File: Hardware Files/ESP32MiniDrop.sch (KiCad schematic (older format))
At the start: 47 parts, among them J1 USB_B_Mini, J2 Barrel_Jack, J3 AudioJack3, J4 Solenoid? Terminal, J5 PROGRAMMING, Q1 S8050, Q2 S8050, Q3 NMOS 60V 46A, SW1 SPST (RED), SW2 SPST (BLUE)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

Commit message: Cleanup Schematics
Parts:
- J4: value Solenoid? Terminal -> Solenoid1 Terminal
- J5: value PROGRAMMING -> 0.100\" 2x4 Header
- R1, R10, R13, R16, R2, R6, R7: value 10k -> 10k 1% 0.1W
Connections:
- net labels added: PairSwitch_CTLI
- net labels removed: PairWitch_CTLI
- wire segments 182 -> 179
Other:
- note added: "18A Max"
- note added: "1A Max"
- note added: "A resistor divider (or functionally-equivalent circuit) on VBUS\nis required to reduce input voltage below maximimum. \nIn this case, the current limitation of the resistor divider \nprevents high VBUS pin leakage current, even \nthough the VIO + 2.5 V specification is not strictly met while\nthe device is not powered."
- note added: "Camera Connection"
- note added: "Camera I/O"
- note added: "D7 must be mounted in reverse. Fixed in Rev A02."
- note added: "EN"
- note added: "ERRATA"
- note added: "IO 0"
- note added: "Lowest current rating is for flyback diode, which could see spikes of\ncurrent equal to the operating current of the coil. 5A at 12V provides \nmaximum of 60 Watts. Typical 12v solenoid is 6.5 Watts. \n\nPlan for testing inductive load at 50 Watts for 20% safety margin.\n\nThrough Hole diodes rated at 100V 20A are available, at marginal\nincrase in cost."
- note added: "MCU"
- note added: "Most DSLR cameras have a 2.5mm TRS port on the camera body to\nallow remote Shutter and Focus control. Different models might have\nShutter and Focus switched, so software might require switching pin\nfunction."
- note added: "NOTE:\nNeed to test LED current with no\ncurrent limiting resisitor in place.\nExpect to damage some LEDs"
- note added: "NOTES"
- note added: "Power Input"
- note added: "Programming Header"
- note added: "REV A01"
- note added: "Regulator for both 12V and 5V\ninput sources"
- note added: "Solenoid Control"
- note added: "Status LEDs"
- note added: "Testing USB to UART chip as found on ESP32 Dev Kit to allow for\nautomatic programing with the Arduino IDE. If that fails, back up\nprogramming header can be used, with jumpers to implement\nboot selection"
- note added: "Theoretical Maximum Power for Solenoid"
- note added: "To enter programming mode"
- note added: "U1 Bypass Capacitors"
- note added: "U3 Bypass Capacitors"
- note added: "User Pair Switch"
- note removed: "Regulator for both 12V and 5V"
- moved on the sheet: C1, C2, C3, C4, C5, C6, C7, C8, C9, D1, D2, D3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

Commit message: Update wrong PN for Green LED
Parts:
- D3: MF Wurth -> Wurth Elektronik; MPN MBR120VLSFT3G -> 150120GS75000
- D4: MF Würth Elektronik -> Wurth Elektronik
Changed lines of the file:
@@
 F 2 "LED_SMD:LED_1206_3216Metric_Pad1.42x1.75mm_HandSolder" H 11100 4050 50  0001 C CNN
 F 3 "~" H 11100 4050 50  0001 C CNN
-F 4 "Würth Elektronik" H 11100 4050 50  0001 C CNN "MF"
+F 4 "Wurth Elektronik" H 11100 4050 50  0001 C CNN "MF"
 F 5 "150120BS75000" H 11100 4050 50  0001 C CNN "MPN"
 	1    11100 4050
@@
 F 2 "LED_SMD:LED_1206_3216Metric_Pad1.42x1.75mm_HandSolder" H 11100 3550 50  0001 C CNN
 F 3 "~" H 11100 3550 50  0001 C CNN
-F 4 "Wurth" H 11100 3550 50  0001 C CNN "MF"
-F 5 "MBR120VLSFT3G" H 11100 3550 50  0001 C CNN "MPN"
+F 4 "Wurth Elektronik" H 11100 3550 50  0001 C CNN "MF"
+F 5 "150120GS75000" H 11100 3550 50  0001 C CNN "MPN"
 	1    11100 3550
 	1    0    0    -1

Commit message: Update project footprint library
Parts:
- J2: footprint ESP32 Drop Controller:PJ-037A -> ESP32MiniDrop_PCB_Library:PJ-037A
- J3: footprint ESP32 Drop Controller:STX-3000 -> ESP32MiniDrop_PCB_Library:STX-3000
- J4: footprint ESP32 Drop Controller:1935161 -> ESP32MiniDrop_PCB_Library:1935161
- SW1, SW2: footprint ESP32 Drop Controller:1825027-8 -> ESP32MiniDrop_PCB_Library:1825027-8
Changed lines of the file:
@@
 F 0 "J4" H 13980 6692 50  0000 L CNN
 F 1 "Solenoid1 Terminal" H 13980 6601 50  0000 L CNN
-F 2 "ESP32 Drop Controller:1935161" H 13900 6700 50  0001 C CNN
+F 2 "ESP32MiniDrop_PCB_Library:1935161" H 13900 6700 50  0001 C CNN
 F 3 "~" H 13900 6700 50  0001 C CNN
 F 4 "Pheonix Contact" H 13900 6700 50  0001 C CNN "MF"
@@
 F 0 "SW1" H 4500 6810 50  0000 C CNN
 F 1 "SPST (RED)" H 4500 6719 50  0000 C CNN
-F 2 "ESP32 Drop Controller:1825027-8" H 4500 6725 50  0001 C CNN
+F 2 "ESP32MiniDrop_PCB_Library:1825027-8" H 4500 6725 50  0001 C CNN
 F 3 "~" H 4500 6725 50  0001 C CNN
 F 4 "TE Connectivity ALCOSWITCH Switches" H 4500 6525 50  0001 C CNN "MF"
@@
 F 0 "J2" H 1320 9700 50  0000 R CNN
 F 1 "Barrel_Jack" H 1320 9609 50  0000 R CNN
-F 2 "ESP32 Drop Controller:PJ-037A" H 1600 9610 50  0001 C CNN
+F 2 "ESP32MiniDrop_PCB_Library:PJ-037A" H 1600 9610 50  0001 C CNN
 F 3 "" H 1600 9610 50  0001 C CNN
 F 4 "CUI Devices" H 1550 9650 50  0001 C CNN "MF"
@@
 F 0 "SW2" H 11700 2535 50  0000 C CNN
 F 1 "SPST (BLUE)" H 11700 2444 50  0000 C CNN
-F 2 "ESP32 Drop Controller:1825027-8" H 11700 2450 50  0001 C CNN
+F 2 "ESP32MiniDrop_PCB_Library:1825027-8" H 11700 2450 50  0001 C CNN
 F 3 "~" H 11700 2450 50  0001 C CNN
 F 4 "TE Connectivity ALCOSWITCH Switches" H 11700 2250 50  0001 C CNN "MF"
@@
 F 0 "J3" H 9170 7075 50  0000 R CNN
 F 1 "AudioJack3" H 9170 6984 50  0000 R CNN
-F 2 "ESP32 Drop Controller:STX-3000" H 9450 7050 50  0001 C CNN
+F 2 "ESP32MiniDrop_PCB_Library:STX-3000" H 9450 7050 50  0001 C CNN
 F 3 "~" H 9450 7050 50  0001 C CNN
 F 4 "Kycon, Inc." H 9450 7050 50  0001 C CNN "MF"

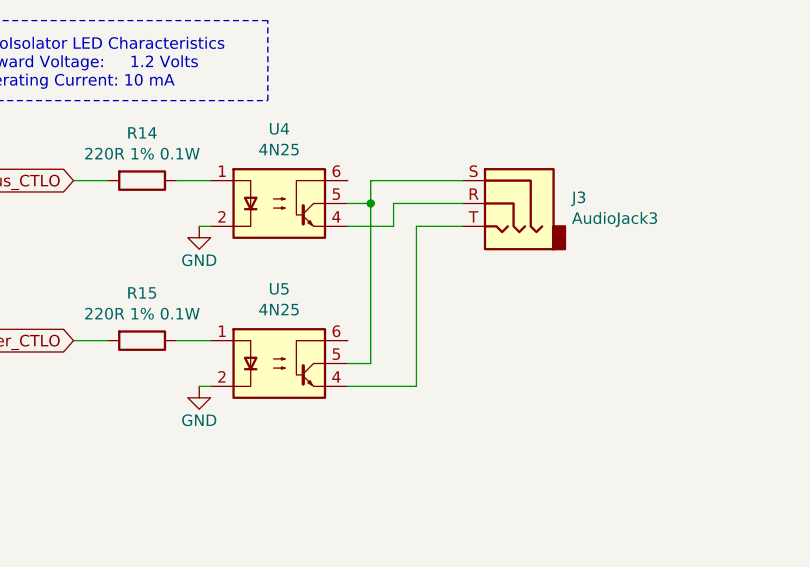
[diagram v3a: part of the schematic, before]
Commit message: fix shutter control hookup
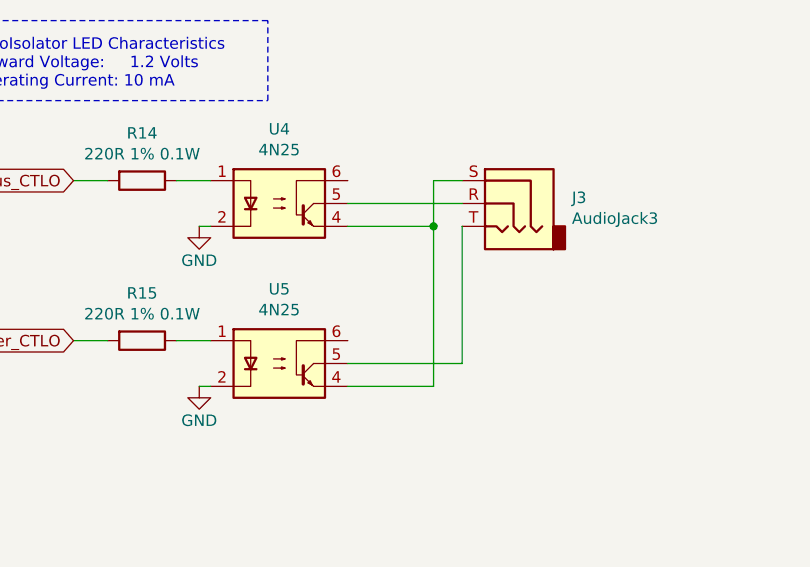
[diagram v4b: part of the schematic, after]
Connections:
- wire segments 179 -> 176
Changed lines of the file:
@@
 	1    0    0    -1
 $EndComp
-Wire Wire Line
-	9250 7050 8950 7050
-Wire Wire Line
-	8950 7050 8950 7150
-Wire Wire Line
-	8950 7150 8750 7150
-Wire Wire Line
-	9250 7150 9050 7150
-Wire Wire Line
-	9050 7850 8750 7850
-Wire Wire Line
-	8750 7750 8850 7750
-Wire Wire Line
-	8850 7050 8750 7050
-Wire Wire Line
-	8850 7050 8850 6950
-Wire Wire Line
-	8850 6950 9250 6950
 Text GLabel 7550 7650 0    50   Input ~ 0
 Shutter_CTLO
@@
 Wire Wire Line
 	8100 7850 8150 7850
-Wire Wire Line
-	8850 7050 8850 7750
-Connection ~ 8850 7050
-Wire Wire Line
-	9050 7150 9050 7850
 Text Notes 7100 6550 0    50   ~ 0
 OptoIsolator LED Characteristics\nForward Voltage:     1.2 Volts\nOperating Current: 10 mA
@@
 Text Notes 11300 4450 0    50   ~ 0
 NOTE:\nNeed to test LED current with no\ncurrent limiting resisitor in place.\nExpect to damage some LEDs
+Wire Wire Line
+	9125 7850 9125 7150
+Wire Wire Line
+	8750 7850 9125 7850
+Wire Wire Line
+	9250 6950 9125 6950
+Wire Wire Line
+	9125 6950 9125 7150
+Connection ~ 9125 7150
+Wire Wire Line
+	8750 7150 9125 7150
+Wire Wire Line
+	8750 7050 9250 7050
+Wire Wire Line
+	9250 7150 9250 7750
+Wire Wire Line
+	9250 7750 8750 7750
 $EndSCHEMATC

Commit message: Fix pin mapping error on Q1, Q2
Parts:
- Q1, Q2: symbol Transistor_BJT:S8050 -> Device:Q_NPN_BEC
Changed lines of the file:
@@
 	950  3500 1000 3500
 $Comp
-L Transistor_BJT:S8050 Q?
+L Device:Q_NPN_BEC Q?
 U 1 1 5F512BB3
 P 1725 6025
@@
 	1825 5825 1825 5775
 $Comp
-L Transistor_BJT:S8050 Q?
+L Device:Q_NPN_BEC Q?
 U 1 1 5F512BC6
 P 1725 6775

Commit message: Change mounting holes to M3, update tracks, change solenoid control to pin 8 of ESP32
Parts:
- added M1, M2, M3, M4: Conn_01x01, MountingHole:MountingHole_3.2mm_M3_ISO7380_Pad, symbol Connector_Generic:Conn_01x01
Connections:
- wire segments 176 -> 184
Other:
- note added: "Mounting Holes"
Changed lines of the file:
@@
 Text GLabel 12850 7350 0    50   Input ~ 0
 Solenoid_1_CTLO
-Text GLabel 9400 3900 2    50   Input ~ 0
+Text GLabel 9400 3700 2    50   Input ~ 0
 Solenoid_1_CTLO
 $Comp
@@
 Wire Wire Line
 	9500 2600 9150 2600
-Wire Wire Line
-	9150 3900 9400 3900
 Text Label 4875 2850 2    50   ~ 0
 USB_TX
@@
 Wire Wire Line
 	9250 7750 8750 7750
+Wire Wire Line
+	9150 3700 9400 3700
+$Comp
+L Connector_Generic:Conn_01x01 M1
+U 1 1 5F5962A4
+P 17475 1250
+F 0 "M1" H 17625 1250 50  0000 C CNN
+F 1 "Conn_01x01" H 17393 1116 50  0001 C CNN
+F 2 "MountingHole:MountingHole_3.2mm_M3_ISO7380_Pad" H 17475 1250 50  0001 C CNN
+F 3 "~" H 17475 1250 50  0001 C CNN
+	1    17475 1250
+	-1   0    0    1
+$EndComp
+$Comp
+L Connector_Generic:Conn_01x01 M2
+U 1 1 5F5A0DC7
+P 17475 1375
+F 0 "M2" H 17625 1375 50  0000 C CNN
+F 1 "Conn_01x01" H 17393 1241 50  0001 C CNN
+F 2 "MountingHole:MountingHole_3.2mm_M3_ISO7380_Pad" H 17475 1375 50  0001 C CNN
+F 3 "~" H 17475 1375 50  0001 C CNN
+	1    17475 1375
+	-1   0    0    1
+$EndComp
+$Comp
+L Connector_Generic:Conn_01x01 M3
+U 1 1 5F5A10F3
+P 17475 1500
+F 0 "M3" H 17625 1500 50  0000 C CNN
+F 1 "Conn_01x01" H 17393 1366 50  0001 C CNN
+F 2 "MountingHole:MountingHole_3.2mm_M3_ISO7380_Pad" H 17475 1500 50  0001 C CNN
+F 3 "~" H 17475 1500 50  0001 C CNN
+	1    17475 1500
+	-1   0    0    1
+$EndComp
+$Comp
+L Connector_Generic:Conn_01x01 M4
+U 1 1 5F5A143F
+P 17475 1625
+F 0 "M4" H 17625 1625 50  0000 C CNN
+F 1 "Conn_01x01" H 17393 1491 50  0001 C CNN
+F 2 "MountingHole:MountingHole_3.2mm_M3_ISO7380_Pad" H 17475 1625 50  0001 C CNN
+F 3 "~" H 17475 1625 50  0001 C CNN
+	1    17475 1625
+	-1   0    0    1
+$EndComp
+$Comp
+L power:GND #PWR0102
+U 1 1 5F5AAE85
+P 17750 1700
+F 0 "#PWR0102" H 17750 1450 50  0001 C CNN
+F 1 "GND" H 17755 1527 50  0000 C CNN
+F 2 "" H 17750 1700 50  0001 C CNN
+F 3 "" H 17750 1700 50  0001 C CNN
+	1    17750 1700
+	1    0    0    -1
+$EndComp
+Wire Wire Line
+	17675 1250 17750 1250
+Wire Wire Line
+	17750 1250 17750 1375
+Wire Wire Line
+	17675 1375 17750 1375
+Connection ~ 17750 1375
+Wire Wire Line
+	17750 1375 17750 1500
+Wire Wire Line
+	17675 1500 17750 1500
+Connection ~ 17750 1500
+Wire Wire Line
+	17750 1500 17750 1625
+Wire Wire Line
+	17675 1625 17750 1625
+Connection ~ 17750 1625
+Wire Wire Line
+	17750 1625 17750 1700
+Text Notes 17000 1025 0    100  ~ 20
+Mounting Holes
 $EndSCHEMATC

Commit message: fix Solenoid MOSFET Pin Mapping
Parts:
- Q3: symbol Device:Q_NMOS_DGS -> Device:Q_NMOS_GDS
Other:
- note removed: "D7 must be mounted in reverse. Fixed in Rev A02."
- note removed: "ERRATA"
- note removed: "REV A01"
- note removed: "Testing USB to UART chip as found on ESP32 Dev Kit to allow for\nautomatic programing with the Arduino IDE. If that fails, back up\nprogramming header can be used, with jumpers to implement\nboot selection"
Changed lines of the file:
@@
 $EndDescr
 $Comp
-L Device:Q_NMOS_DGS Q3
+L Device:Q_NMOS_GDS Q3
 U 1 1 5F4F858B
 P 13300 7350
@@
 Wire Notes Line
 	13250 1800 13300 1800
-Wire Notes Line
-	13125 2445 13125 2495
-Wire Notes Line
-	13125 2495 13175 2495
-Text Notes 13175 2525 0    50   ~ 0
-USB to UART
-Text Notes 13275 2875 0    50   ~ 0
-Testing USB to UART chip as found on ESP32 Dev Kit to allow for\nautomatic programing with the Arduino IDE. If that fails, back up\nprogramming header can be used, with jumpers to implement\nboot selection
-Wire Notes Line
-	13250 2575 13250 2900
-Wire Notes Line
-	13250 2900 13300 2900
 Text Notes 575  5150 0    39   ~ 0
 A resistor divider (or functionally-equivalent circuit) on VBUS\nis required to reduce input voltage below maximimum. \nIn this case, the current limitation of the resistor divider \nprevents high VBUS pin leakage current, even \nthough the VIO + 2.5 V specification is not strictly met while\nthe device is not powered.
@@
 Text Notes 3950 9650 0    50   ~ 0
 1A Max
-Text Notes 13100 3150 0    100  ~ 20
-ERRATA
-Text Notes 13175 3275 0    50   ~ 0
-REV A01
-Text Notes 13275 3375 0    50   ~ 0
-D7 must be mounted in reverse. Fixed in Rev A02.
 Wire Notes Line
 	4275 6075 4750 6075

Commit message: section off Do Not Place parts
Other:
- note added: "DNP"
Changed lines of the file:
@@
 Text Label 9500 1700 2    50   ~ 0
 IO0
-Wire Wire Line
-	9500 1700 9150 1700
 Text Label 2225 3050 0    50   ~ 0
 D+
@@
 Wire Wire Line
 	3700 10000 4450 10000
-Text Notes 1300 8900 0    50   ~ 0
+Text Notes 1075 8600 0    50   ~ 0
 Drop Out Voltage: 1.3V@800mA\nUSB rectified voltage: 4.65V
 $Comp
@@
 Text Notes 17000 1025 0    100  ~ 20
 Mounting Holes
+Wire Notes Line rgb(0, 132, 0)
+	525  525  5175 525
+Wire Notes Line rgb(0, 132, 0)
+	5175 525  5175 5425
+Wire Notes Line rgb(0, 132, 0)
+	5175 5425 525  5425
+Wire Notes Line rgb(0, 132, 0)
+	525  5425 525  525
+Text Notes 4700 750  0    118  ~ 24
+DNP
+Wire Notes Line
+	2175 5650 2175 7150
+Wire Notes Line
+	2175 7150 850  7150
+Wire Notes Line
+	850  7150 850  5650
+Wire Notes Line
+	850  5650 2175 5650
+Wire Notes Line
+	2800 9250 2800 8850
+Wire Notes Line
+	2800 8850 2175 8850
+Wire Notes Line
+	2175 8850 2175 9250
+Wire Notes Line
+	2175 9250 2800 9250
+Wire Wire Line
+	9500 1700 9150 1700
 $EndSCHEMATC
